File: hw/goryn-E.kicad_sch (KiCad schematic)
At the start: 8 parts, among them J3 Conn_01x34, U2 W25Q128JVS

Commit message: added DC-DC
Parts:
- added C10, C11, C12: 22uF, AI6YP:C_0603_1608Metric, symbol AI6YP:C
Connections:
- net +1V0: now also C10.1, C12.1
- net +3V3: now also C11.1
- net GND: now also C10.2, C11.2, C12.2
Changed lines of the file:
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@@
+    (stroke (width 0) (type default))
+  )
+  (wire (pts (xy 125 199) (xy 125 201))
     (stroke (width 0) (type default))
   )
@@
     (stroke (width 0) (type default))
   )
+  (wire (pts (xy 134 194) (xy 134 197))
+    (stroke (width 0) (type default))
+  )
   (wire (pts (xy 100 108) (xy 146 108))
     (stroke (width 0) (type default))
   )
+  (wire (pts (xy 130 63) (xy 130 65))
+    (stroke (width 0) (type default))
+  )
   (wire (pts (xy 100 192) (xy 103 192))
     (stroke (width 0) (type default))
@@
     (stroke (width 0) (type default))
   )
+  (wire (pts (xy 134 199) (xy 134 201))
+    (stroke (width 0) (type default))
+  )
   (wire (pts (xy 100 164) (xy 103 164))
     (stroke (width 0) (type default))
@@
   )
   (wire (pts (xy 100 112) (xy 146 112))
+    (stroke (width 0) (type default))
+  )
+  (wire (pts (xy 130 58) (xy 130 61))
+    (stroke (width 0) (type default))
+  )
+  (wire (pts (xy 125 194) (xy 125 197))
     (stroke (width 0) (type default))
   )
@@
     )
   )
+  (symbol (lib_id "AI6YP:GND") (at 130 65 0) (unit 1)
+    (in_bom yes) (on_board yes) (dnp no) (fields_autoplaced)
+    (property "Reference" "#PWR0106" (at 130 69 0)
+      (effects (font (size 1 1)) hide)
+    )
+    (property "Value" "GND" (at 130 68.22 0)
+      (effects (font (size 1 1)))
+    )
+    (property "Footprint" "" (at 130 65 0)
+      (effects (font (size 1 1)) hide)
+    )
+    (property "Datasheet" "" (at 130 65 0)
+      (effects (font (size 1 1)) hide)
+    )
+    (pin "1")
+    (instances
+      (project "goryn"
+        (path "/745fe258-3c32-4527-ad01-ef9d3fd5a8f9/c39836a0-69bd-42e3-a86b-0989a6330659"
+          (reference "#PWR0106") (unit 1)
+        )
+      )
+    )
+  )
   (symbol (lib_id "AI6YP:+3V3") (at 152 216 270) (unit 1)
     (in_bom yes) (on_board yes) (dnp no) (fields_autoplaced)
@@
         (path "/745fe258-3c32-4527-ad01-ef9d3fd5a8f9/c39836a0-69bd-42e3-a86b-0989a6330659"
           (reference "#PWR049") (unit 1)
+        )
+      )
+    )
+  )
+  (symbol (lib_id "AI6YP:C") (at 130 62 0) (unit 1)
+    (in_bom yes) (on_board yes) (dnp no)
+    (property "Reference" "C10" (at 131 61 0)
+      (effects (font (size 1 1)) (justify left))
+    )
+    (property "Value" "22uF" (at 131 63 0)
+      (effects (font (size 1 1)) (justify left))
+    )
+    (property "Footprint" "AI6YP:C_0603_1608Metric" (at 131 66 0)
+      (effects (font (size 1 1)) hide)
+    )
+    (property "Datasheet" "~" (at 130 62 0)
+      (effects (font (size 1 1)) hide)
+    )
+    (pin "1")
+    (pin "2")
+    (instances
+      (project "goryn"
+        (path "/745fe258-3c32-4527-ad01-ef9d3fd5a8f9/c39836a0-69bd-42e3-a86b-0989a6330659"
+          (reference "C10") (unit 1)
         )
       )
@@
     )
   )
+  (symbol (lib_id "AI6YP:+3V3") (at 125 194 0) (unit 1)
+    (in_bom yes) (on_board yes) (dnp no) (fields_autoplaced)
+    (property "Reference" "#PWR0107" (at 125 196 0)
+      (effects (font (size 1 1)) hide)
+    )
+    (property "Value" "+3V3" (at 125 190.28 0)
+      (effects (font (size 1 1)))
+    )
+    (property "Footprint" "" (at 125 194 0)
+      (effects (font (size 1 1)) hide)
+    )
+    (property "Datasheet" "" (at 125 194 0)
+      (effects (font (size 1 1)) hide)
+    )
+    (pin "1")
+    (instances
+      (project "goryn"
+        (path "/745fe258-3c32-4527-ad01-ef9d3fd5a8f9/c39836a0-69bd-42e3-a86b-0989a6330659"
+          (reference "#PWR0107") (unit 1)
+        )
+      )
+    )
+  )
   (symbol (lib_id "AI6YP:GND") (at 103 92 90) (unit 1)
     (in_bom yes) (on_board yes) (dnp no) (fields_autoplaced)
@@
         (path "/745fe258-3c32-4527-ad01-ef9d3fd5a8f9/c39836a0-69bd-42e3-a86b-0989a6330659"
           (reference "#PWR028") (unit 1)
+        )
+      )
+    )
+  )
+  (symbol (lib_id "AI6YP:GND") (at 134 201 0) (unit 1)
+    (in_bom yes) (on_board yes) (dnp no) (fields_autoplaced)
+    (property "Reference" "#PWR0110" (at 134 205 0)
+      (effects (font (size 1 1)) hide)
+    )
+    (property "Value" "GND" (at 134 204.22 0)
+      (effects (font (size 1 1)))
+    )
+    (property "Footprint" "" (at 134 201 0)
+      (effects (font (size 1 1)) hide)
+    )
+    (property "Datasheet" "" (at 134 201 0)
+      (effects (font (size 1 1)) hide)
+    )
+    (pin "1")
+    (instances
+      (project "goryn"
+        (path "/745fe258-3c32-4527-ad01-ef9d3fd5a8f9/c39836a0-69bd-42e3-a86b-0989a6330659"
+          (reference "#PWR0110") (unit 1)
         )
       )
@@
         )
       )
+    )
+  )
+  (symbol (lib_id "AI6YP:GND") (at 125 201 0) (unit 1)
+    (in_bom yes) (on_board yes) (dnp no) (fields_autoplaced)
+    (property "Reference" "#PWR0108" (at 125 205 0)
+      (effects (font (size 1 1)) hide)
+    )
+    (property "Value" "GND" (at 125 204.22 0)
+      (effects (font (size 1 1)))
+    )
+    (property "Footprint" "" (at 125 201 0)
+      (effects (font (size 1 1)) hide)
+    )
+    (property "Datasheet" "" (at 125 201 0)
+      (effects (font (size 1 1)) hide)
+    )
+    (pin "1")
+    (instances
+      (project "goryn"
+        (path "/745fe258-3c32-4527-ad01-ef9d3fd5a8f9/c39836a0-69bd-42e3-a86b-0989a6330659"
+          (reference "#PWR0108") (unit 1)
+        )
+      )
+    )
+  )
+  (symbol (lib_id "AI6YP:C") (at 134 198 0) (unit 1)
+    (in_bom yes) (on_board yes) (dnp no)
+    (property "Reference" "C12" (at 135 197 0)
+      (effects (font (size 1 1)) (justify left))
+    )
+    (property "Value" "22uF" (at 135 199 0)
+      (effects (font (size 1 1)) (justify left))
+    )
+    (property "Footprint" "AI6YP:C_0603_1608Metric" (at 135 202 0)
+      (effects (font (size 1 1)) hide)
+    )
+    (property "Datasheet" "~" (at 134 198 0)
+      (effects (font (size 1 1)) hide)
+    )
+    (pin "1")
+    (pin "2")
+    (instances
+      (project "goryn"
+        (path "/745fe258-3c32-4527-ad01-ef9d3fd5a8f9/c39836a0-69bd-42e3-a86b-0989a6330659"
+          (reference "C12") (unit 1)
+        )
+      )
+    )
+  )
+  (symbol (lib_id "AI6YP:+1V0") (at 134 194 0) (unit 1)
+    (in_bom yes) (on_board yes) (dnp no)
+    (property "Reference" "#PWR0109" (at 134 196 0)
+      (effects (font (size 1 1)) hide)
+    )
+    (property "Value" "+1V0" (at 134 190 0)
+      (effects (font (size 1 1)))
+    )
+    (property "Footprint" "" (at 134 194 0)
+      (effects (font (size 1 1)) hide)
+    )
+    (property "Datasheet" "" (at 134 194 0)
+      (effects (font (size 1 1)) hide)
+    )
+    (pin "1")
+    (instances
+      (project "goryn"
+        (path "/745fe258-3c32-4527-ad01-ef9d3fd5a8f9/c39836a0-69bd-42e3-a86b-0989a6330659"
+          (reference "#PWR0109") (unit 1)
+        )
+      )
+    )
+  )
+  (symbol (lib_id "AI6YP:+1V0") (at 130 58 0) (unit 1)
+    (in_bom yes) (on_board yes) (dnp no) (fields_autoplaced)
+    (property "Reference" "#PWR0105" (at 130 60 0)
+      (effects (font (size 1 1)) hide)
+    )
+    (property "Value" "+1V0" (at 130 54.34 0)
+      (effects (font (size 1 1)))
+    )
+    (property "Footprint" "" (at 130 58 0)
+      (effects (font (size 1 1)) hide)
+    )
+    (property "Datasheet" "" (at 130 58 0)
+      (effects (font (size 1 1)) hide)
+    )
+    (pin "1")
+    (instances
+      (project "goryn"
+        (path "/745fe258-3c32-4527-ad01-ef9d3fd5a8f9/c39836a0-69bd-42e3-a86b-0989a6330659"
+          (reference "#PWR0105") (unit 1)
+        )
+      )
+    )
+  )
+  (symbol (lib_id "AI6YP:C") (at 125 198 0) (unit 1)
+    (in_bom yes) (on_board yes) (dnp no)
+    (property "Reference" "C11" (at 126 197 0)
+      (effects (font (size 1 1)) (justify left))
+    )
+    (property "Value" "22uF" (at 126 199 0)
+      (effects (font (size 1 1)) (justify left))
+    )
+    (property "Footprint" "AI6YP:C_0603_1608Metric" (at 126 202 0)
+      (effects (font (size 1 1)) hide)
+    )
+    (property "Datasheet" "~" (at 125 198 0)
+      (effects (font (size 1 1)) hide)
+    )
+    (pin "1")
+    (pin "2")
+    (instances
+      (project "goryn"
+        (path "/745fe258-3c32-4527-ad01-ef9d3fd5a8f9/c39836a0-69bd-42e3-a86b-0989a6330659"
+          (reference "C11") (unit 1)
+        )
+      )

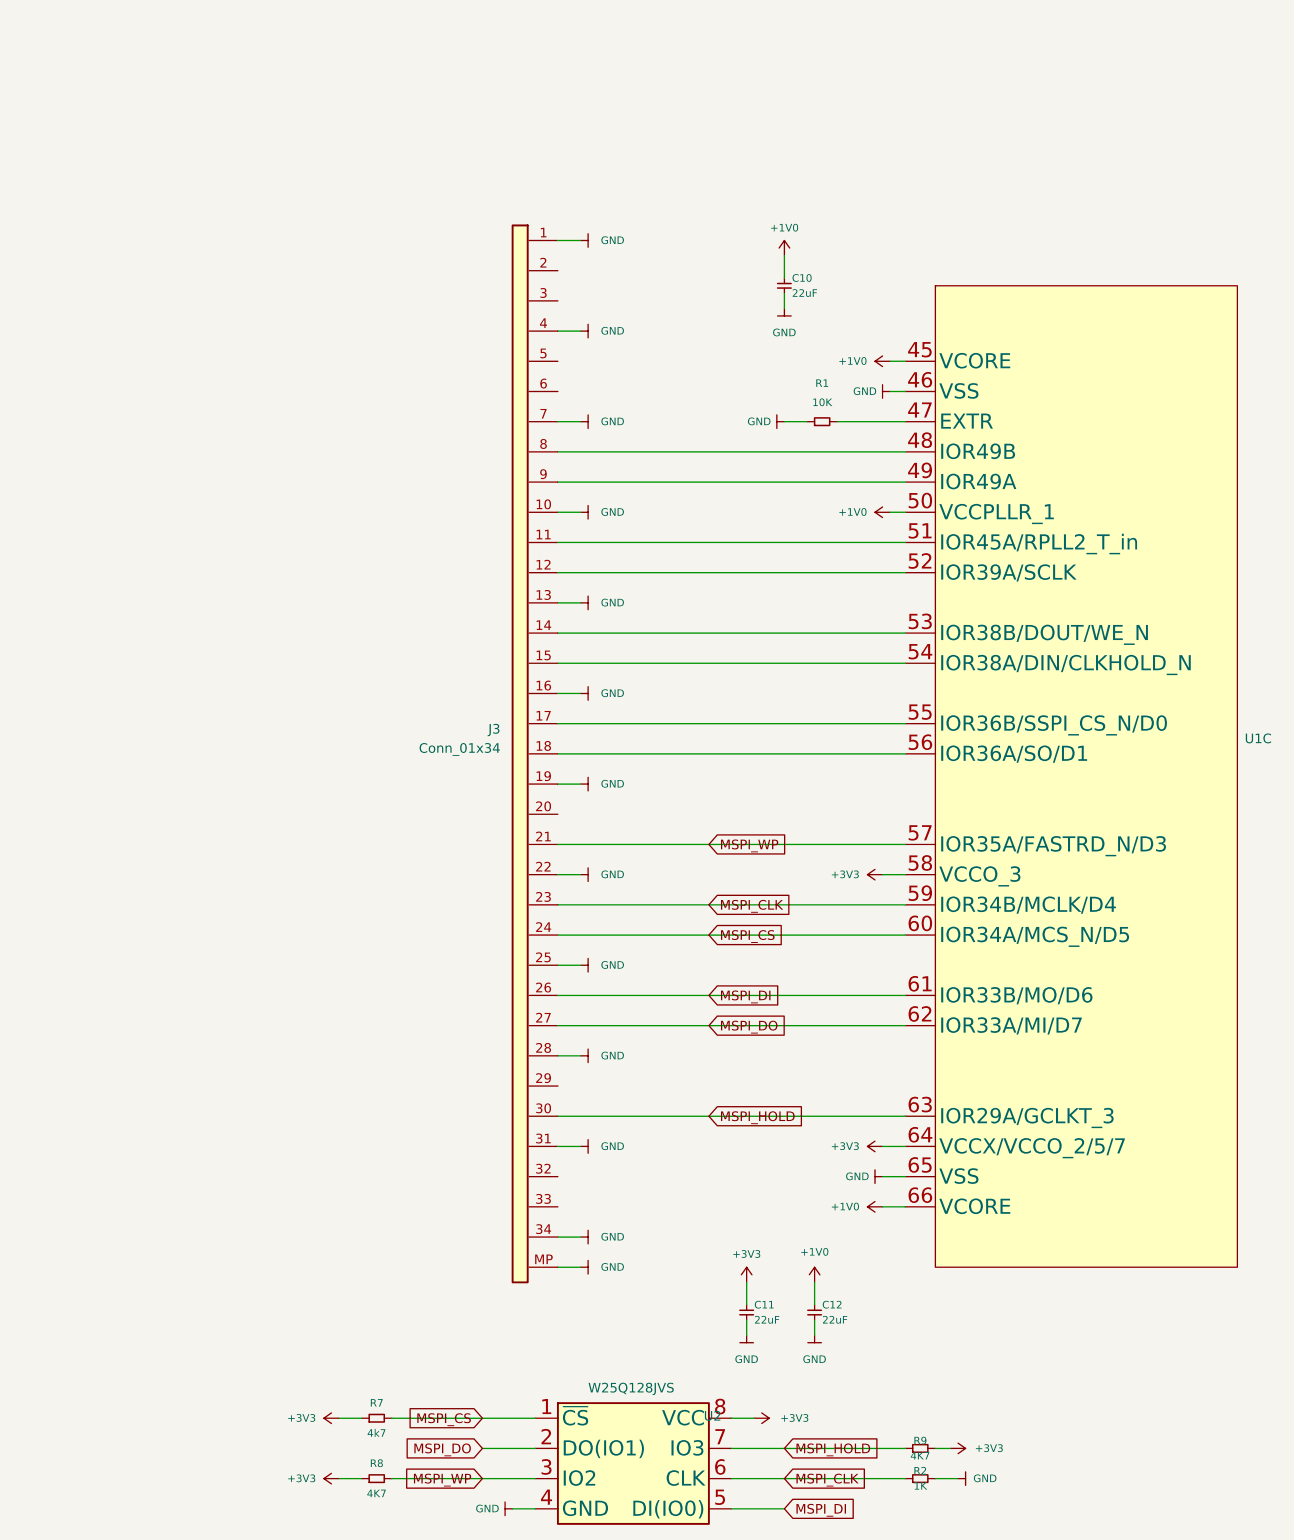
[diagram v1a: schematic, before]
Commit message: FFC34 -> FFC30
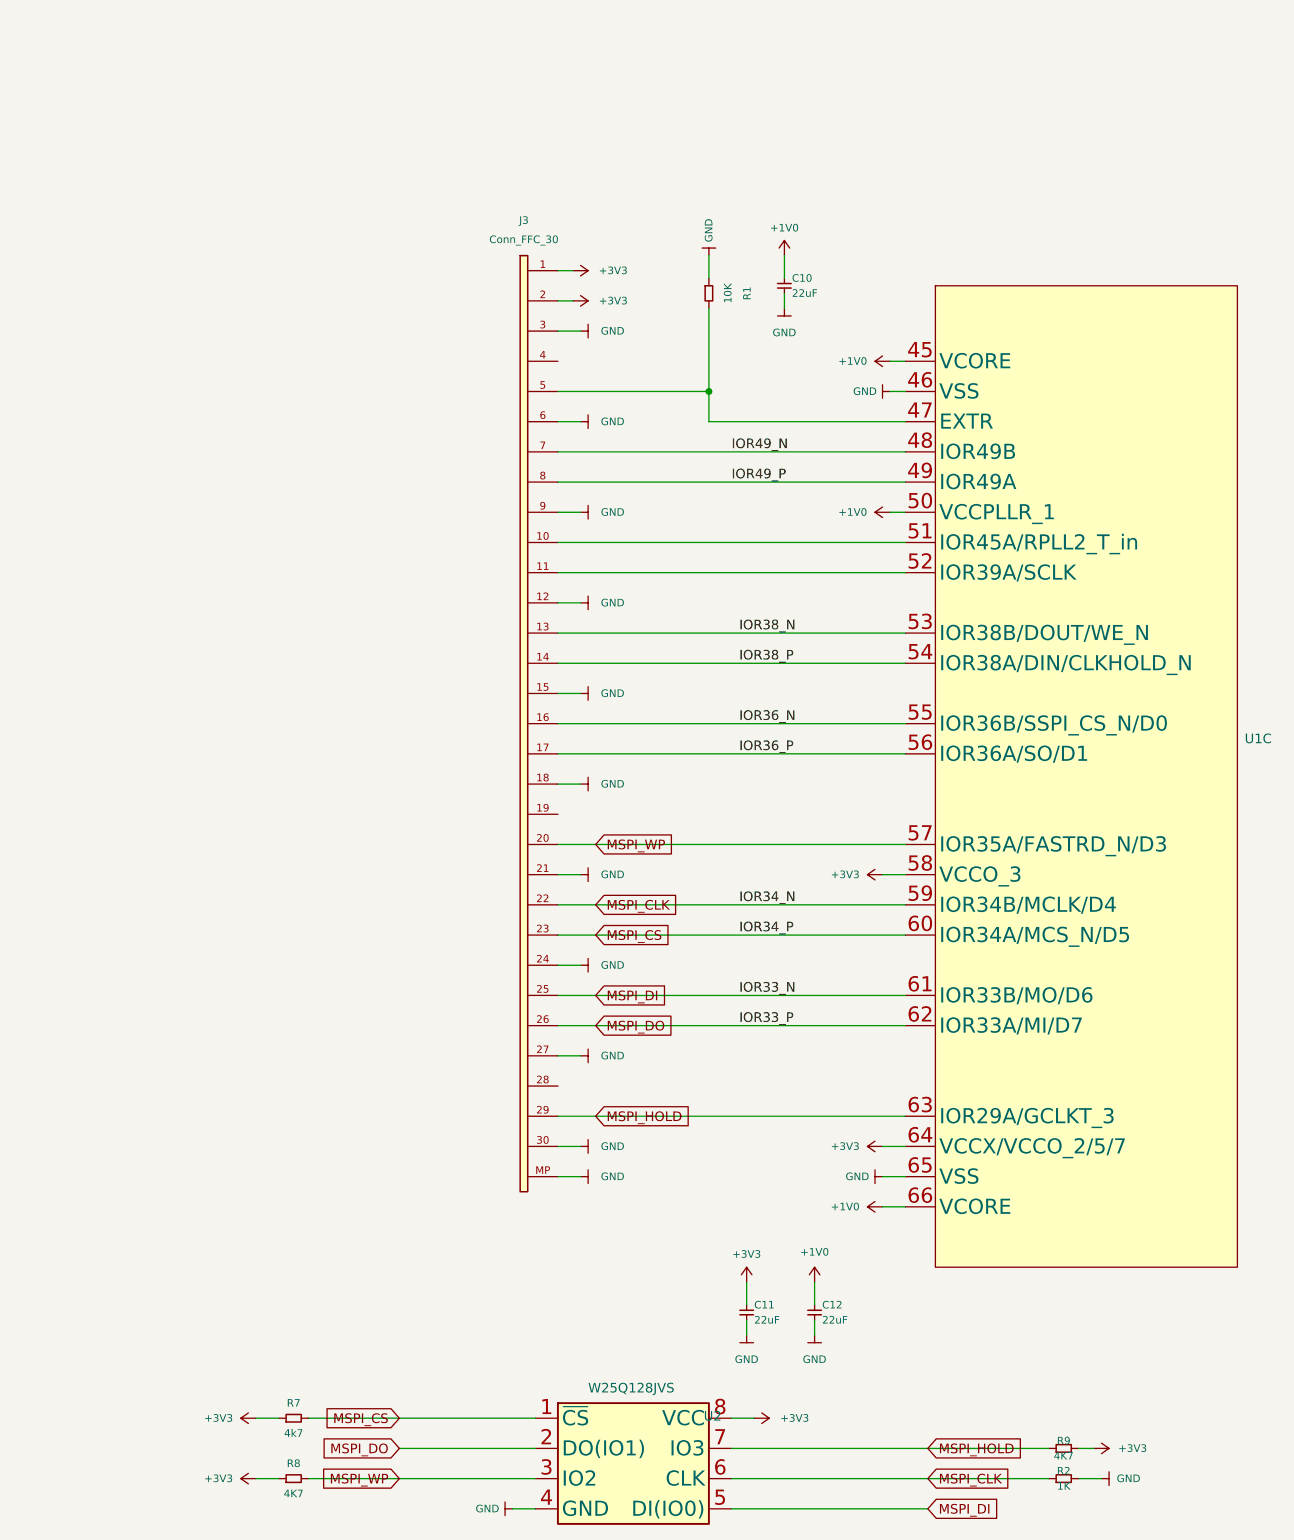
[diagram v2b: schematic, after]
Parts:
- removed J3: Conn_01x34, AI6YP:Hirose_FH12-34S-0.5SH_1x34-1MP_P0.50mm_Horizontal, symbol AI6YP:Conn_01x34
- added J3: Conn_FFC_30, AI6YP:Hirose_FH12-30S-0.5SH_1x30-1MP_P0.50mm_Horizontal, symbol AI6YP:Conn_FFC_30
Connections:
- net +3V3: now also J3.1 (Pin_1), J3.2 (Pin_2)
- net GND: now also J3.12 (Pin_12), J3.15 (Pin_15), J3.18 (Pin_18), J3.21 (Pin_21), J3.24 (Pin_24), J3.27 (Pin_27), J3.3 (Pin_3), J3.30 (Pin_30), J3.6 (Pin_6), J3.9 (Pin_9), J3.MP (Pin_MP)
- net MSPI_CLK: now also J3.22 (Pin_22)
- net MSPI_CS: now also J3.23 (Pin_23)
- net MSPI_DI: now also J3.25 (Pin_25)
- net MSPI_DO: now also J3.26 (Pin_26)
- net MSPI_HOLD: now also J3.29 (Pin_29)
- net MSPI_WP: now also J3.20 (Pin_20)
- net at R1.2, U1.47 (EXTR): now also J3.5 (Pin_5)
- net IOR49_N: now reaches U1.48 (IOR49B)
- net IOR49_N: now also J3.7 (Pin_7)
- net IOR49_P: now reaches U1.49 (IOR49A)
- net IOR49_P: now also J3.8 (Pin_8)
- net at U1.51 (IOR45A/RPLL2_T_in): now also J3.10 (Pin_10)
- net at U1.52 (IOR39A/SCLK): now also J3.11 (Pin_11)
- net IOR38_N: now reaches U1.53 (IOR38B/DOUT/WE_N)
- net IOR38_N: now also J3.13 (Pin_13)
- net IOR38_P: now reaches U1.54 (IOR38A/DIN/CLKHOLD_N)
- net IOR38_P: now also J3.14 (Pin_14)
- net IOR36_N: now reaches U1.55 (IOR36B/SSPI_CS_N/D0)
- net IOR36_N: now also J3.16 (Pin_16)
- net IOR36_P: now reaches U1.56 (IOR36A/SO/D1)
- net IOR36_P: now also J3.17 (Pin_17)
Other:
- moved on the sheet: R1, R2, R7, R8, R9

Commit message: happy kicad 8
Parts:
- added H3: MountingHole_M3, AI6YP:MountingHole_3.2mm_M3_Pad_Via, symbol AI6YP:MountingHole_M3
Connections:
- net +3V3: now also J3.30 (Pin_30); no longer J3.2 (Pin_2)
- net GND: now also J3.11 (Pin_11), J3.14 (Pin_14), J3.17 (Pin_17), J3.2 (Pin_2), J3.20 (Pin_20), J3.23 (Pin_23), J3.26 (Pin_26), J3.29 (Pin_29), J3.5 (Pin_5), J3.8 (Pin_8), H3.1; no longer J3.12 (Pin_12), J3.15 (Pin_15), J3.18 (Pin_18), J3.21 (Pin_21), J3.24 (Pin_24), J3.27 (Pin_27), J3.3 (Pin_3), J3.30 (Pin_30), J3.6 (Pin_6), J3.9 (Pin_9)
- net IOR36_N: now also J3.15 (Pin_15); no longer J3.16 (Pin_16)
- net IOR36_P: now also J3.16 (Pin_16); no longer J3.17 (Pin_17)
- net IOR38_N: now also J3.12 (Pin_12); no longer J3.13 (Pin_13)
- net IOR38_P: now also J3.13 (Pin_13); no longer J3.14 (Pin_14)
- net IOR49_N: now also J3.6 (Pin_6); no longer J3.7 (Pin_7)
- net IOR49_P: now also J3.7 (Pin_7); no longer J3.8 (Pin_8)
- net MSPI_CLK: now also J3.21 (Pin_21); no longer J3.22 (Pin_22)
- net MSPI_CS: now also J3.22 (Pin_22); no longer J3.23 (Pin_23)
- net MSPI_DI: now also J3.24 (Pin_24); no longer J3.25 (Pin_25)
- net MSPI_DO: now also J3.25 (Pin_25); no longer J3.26 (Pin_26)
- net MSPI_HOLD: now also J3.28 (Pin_28); no longer J3.29 (Pin_29)
- net MSPI_WP: now also J3.19 (Pin_19); no longer J3.20 (Pin_20)
- net at J3.10 (Pin_10): now also U1.52 (IOR39A/SCLK); no longer U1.51 (IOR45A/RPLL2_T_in)
- net at R1.2, U1.47 (EXTR): no longer J3.5 (Pin_5)
- new net: J3.9 (Pin_9), U1.51 (IOR45A/RPLL2_T_in)
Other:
- moved on the sheet: C10, C11, C12, J3, R1, U1C

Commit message: finished routing
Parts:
- removed H3: MountingHole_M3, AI6YP:MountingHole_3.2mm_M3_Pad_Via, symbol AI6YP:MountingHole_M3
- added J10: 3V3, AI6YP:PinHeader_1x02_P2.54mm_Vertical, symbol AI6YP:PinHeader_1x02_P2.54mm_Vertical
- added J8: 5V, AI6YP:PinHeader_1x02_P2.54mm_Vertical, symbol AI6YP:PinHeader_1x02_P2.54mm_Vertical
- added J9: 1V, AI6YP:PinHeader_1x02_P2.54mm_Vertical, symbol AI6YP:PinHeader_1x02_P2.54mm_Vertical
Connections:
- net +1V0: now also J9.2 (Pin_2)
- net +3V3: now also J10.2 (Pin_2)
- net GND: now also J10.1 (Pin_1), J8.1 (Pin_1), J9.1 (Pin_1)
- net MSPI_WP: now also J3.18 (Pin_18); no longer J3.19 (Pin_19)
- new net +5V: J8.2 (Pin_2)

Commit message: v1.0.0
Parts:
- added C15: 22uF, AI6YP:C_0603_1608Metric, symbol AI6YP:C
- U1: footprint AI6YP:QFN-88-10x10mm-P0.4mm-EP6.74x6.74mm -> AI6YP:GIWIN-QFN-88-10x10mm-P0.4mm-EP6.74x6.74mm
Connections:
- net +3V3: now also C15.1
- net GND: now also C15.2
- net MSPI_CLK renamed IOR34_N
- net MSPI_CS renamed IOR34_P
- net MSPI_DI renamed IOR33_N
- net MSPI_DO renamed IOR33_P
- net MSPI_HOLD renamed IOR29A
- net MSPI_WP renamed IOR35A
